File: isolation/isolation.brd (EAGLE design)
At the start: 74.5 x 72.7 mm, 88 parts, among them IC1 XTLV61048DBVR, IC2 SN74HC14PWR, IC3 SN74HCS32BQAR, IC4 SN74HCS08DYYR, IC5 FDN359BN, IC6 FDN359BN, IC7 FDN359BN, IC8 FDN359BN, J1 S4B-PH-K-S(LF)(SN), J2 S4B-PH-K-S(LF)(SN), J3 S2B-PH-K-S(LF)(SN), J4 S2B-PH-K-S(LF)(SN), J5 S2B-PH-K-S(LF)(SN), J6 USB4105-GF-A

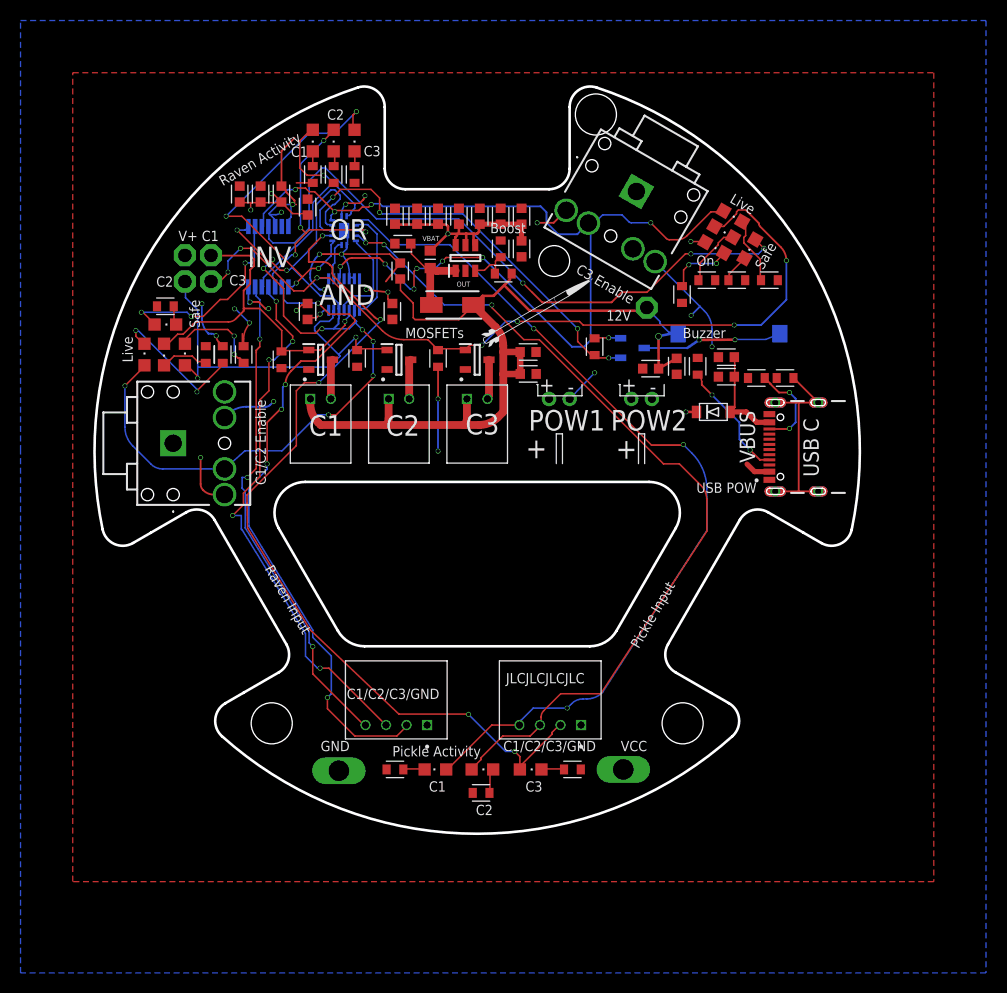
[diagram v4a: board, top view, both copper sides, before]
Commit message: move all components to top
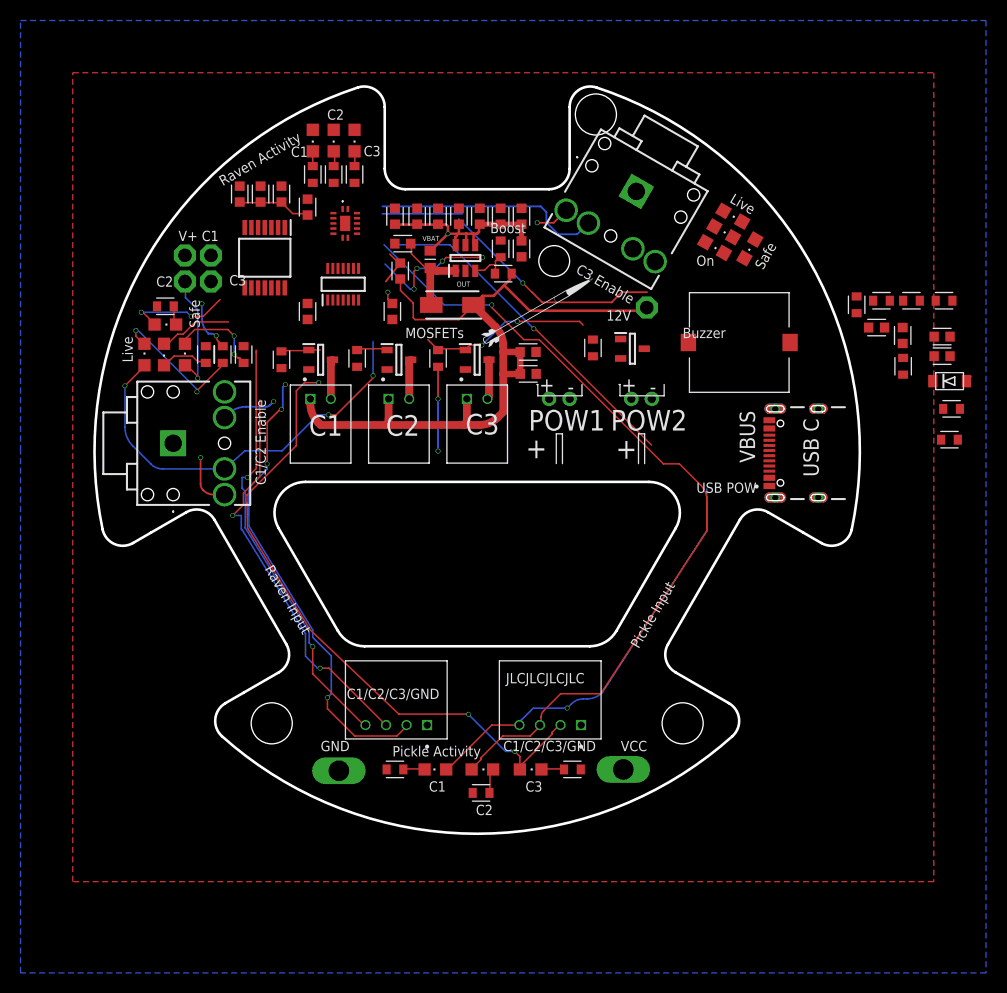
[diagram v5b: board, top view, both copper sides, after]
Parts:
- moved D2 23.2 mm to (46.0, 6.81)
- moved C19 22.4 mm to (38.9, 12.0)
- moved C18 22.2 mm to (41.4, 11.2)
- moved C14 21.1 mm to (45.3, 9.24)
- moved C15 21.1 mm to (45.3, 11.1)
- moved R14 20.0 mm to (41.5, 8.26)
- moved R12 19.2 mm to (46.2, 4.11)
- moved R7 17.1 mm to (42.3, 14.6)
- moved R5 17.1 mm to (45.4, 14.6)
- moved R23 17.1 mm to (39.4, 14.6)
- moved R13 17.1 mm to (46.0, 1.11)
- moved R1 17.0 mm to (36.9, 14.2)
- moved LS1 1.32 mm to (25.5, 10.6), flipped to the top, turned to 90 degrees
- moved IC4 1.00 mm to (-13.0, 16.2), flipped to the top
- moved IC3 0.71 mm to (-12.8, 22.2), flipped to the top
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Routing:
- net EN2: track 99.0 -> 36.0 mm, vias 10 -> 4
- net FIRE3: track 80.7 -> 17.9 mm, vias 7 -> 2
- net GND: track 82.6 -> 22.8 mm, vias 17 -> 5
- net EN1: track 90.7 -> 40.2 mm, vias 10 -> 3
- net SAFE2: track 64.1 -> 22.3 mm, vias 3 -> 1
- net INVR3: track 35.8 -> 0.15 mm, vias 4 -> 0
- net BUZZ: track 41.4 -> 8.10 mm, vias 4 -> 0
- net INVR1: track 26.1 -> 0.52 mm, vias 1 -> 0
- net INVR2: track 25.6 -> 0.18 mm, vias 4 -> 0
- net FIRE2: track 39.7 -> 15.1 mm, vias 2 -> 1
- net FIRE1: track 34.2 -> 11.0 mm, vias 1 -> 0
- net PICKLE3: track 84.5 -> 62.2 mm, vias 5 -> 3
- net SHLD: track 20.4 -> 0.02 mm
- net RAVEN3: track 64.1 -> 45.2 mm, vias 5 -> 4
- net VBAT: track 55.8 -> 40.3 mm, vias 14 -> 4
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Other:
- board text removed: "AND"
- board text removed: "INV"
- board text removed: "OR"

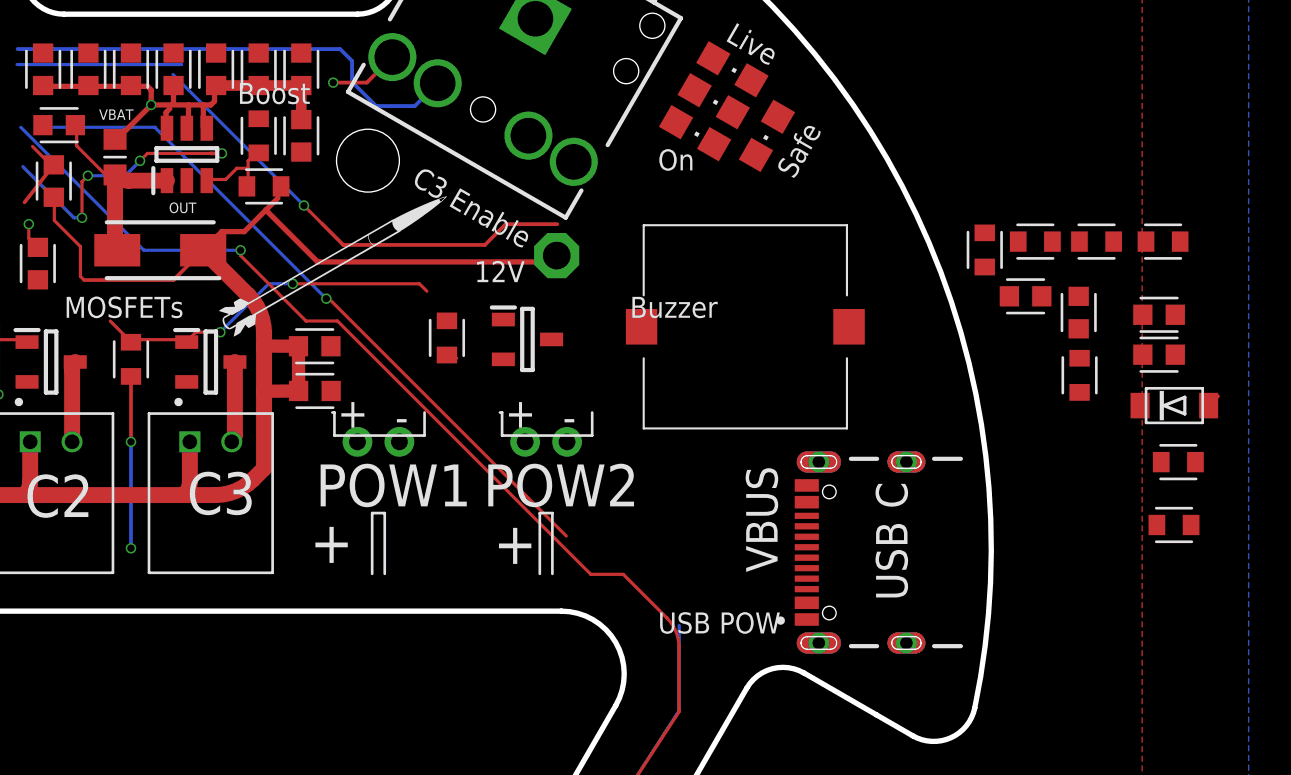
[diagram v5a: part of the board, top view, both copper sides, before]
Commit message: flip all components to top
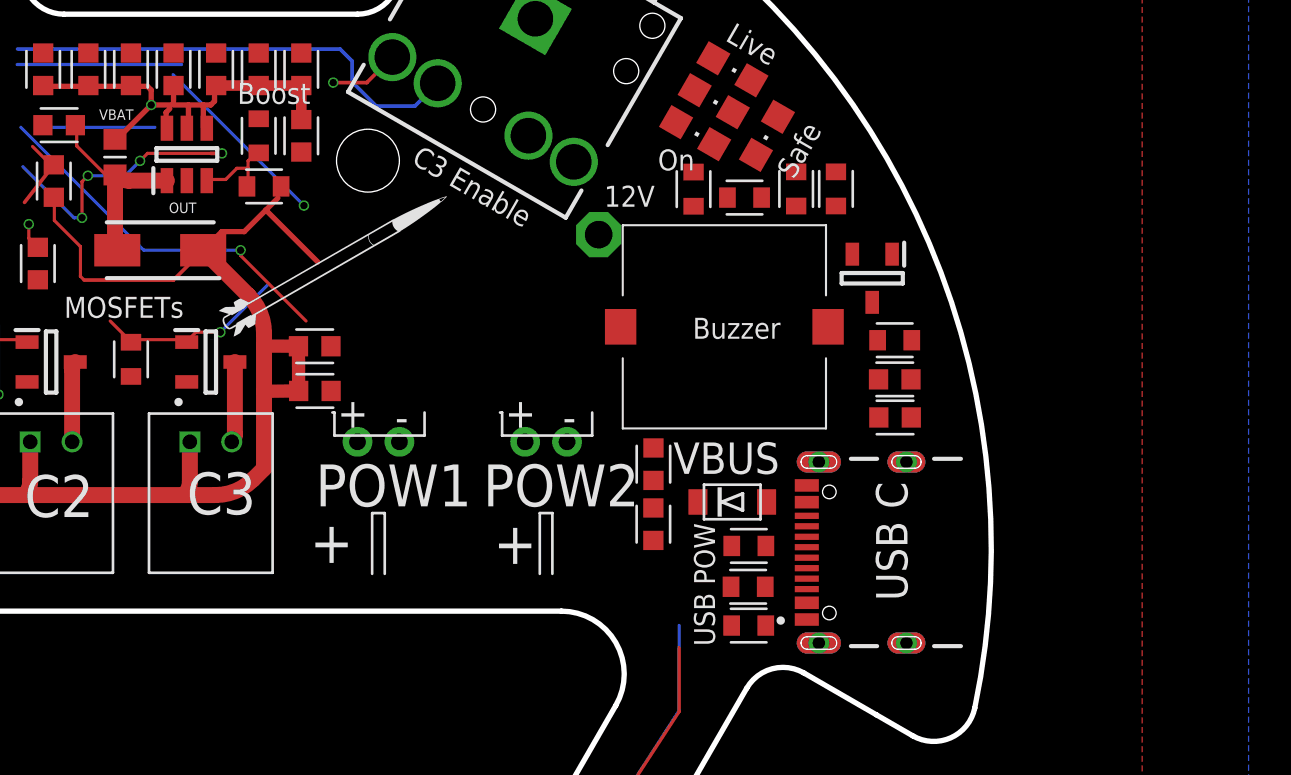
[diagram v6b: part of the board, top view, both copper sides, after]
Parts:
- moved C18 22.7 mm to (21.1, 1.15)
- moved D2 21.6 mm to (24.9, 2.21)
- moved R11 21.4 mm to (32.6, 9.93), turned to 180 degrees
- moved R12 20.9 mm to (25.7, 0.11)
- moved R13 20.9 mm to (25.7, -3.69)
- moved C19 19.5 mm to (21.1, 4.01), turned to 90 degrees
- moved R14 18.8 mm to (25.6, -1.84), turned to 180 degrees
- moved R7 16.9 mm to (25.5, 16.7)
- moved IC8 16.7 mm to (31.6, 12.9), turned to 270 degrees
- moved R5 15.8 mm to (29.8, 17.2), turned to 90 degrees
- moved R1 14.2 mm to (23.0, 17.1)
- moved C15 13.5 mm to (32.7, 6.24), turned to 180 degrees
- moved C14 12.7 mm to (32.6, 8.06), turned to 180 degrees
- moved R23 11.7 mm to (27.9, 17.1), turned to 90 degrees
- moved TP9 2.24 mm to (18.5, 15.0)
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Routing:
- net PICKLE1: track 74.3 -> 46.5 mm, vias 2 -> 1
- net PICKLE2: track 80.6 -> 56.0 mm
- net SAFE2: track 22.3 -> 9.04 mm
- net VDEP: track 73.7 -> 62.6 mm
- net GND: track 22.8 -> 14.5 mm, vias 5 -> 3
- net FIRE3: track 17.9 -> 10.2 mm, vias 2 -> 1
- net VBUS: track 0.91 -> 0.00 mm

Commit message: reset layout
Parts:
- moved C13 3.12 mm to (-9.65, 16.4)
- moved C12 1.27 mm to (-16.5, 12.3), turned to 180 degrees
- moved IC2 1.27 mm to (-20.7, 17.6)
- moved C11 0.36 mm to (-16.3, 24.0)
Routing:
- net VBAT: track 40.3 -> 0.00 mm, vias 4 -> 0
- net EN1: track 40.2 -> 0.00 mm, vias 3 -> 0
- net EN2: track 36.0 -> 0.00 mm, vias 4 -> 0
- net VDEP: track 62.6 -> 39.6 mm
- net PICKLE1: track 46.5 -> 69.0 mm
- net VBUS: track 0.00 -> 16.2 mm
- net SHLD: track 0.00 -> 15.7 mm
- net FIRE2: track 15.1 -> 0.00 mm, vias 1 -> 0
- net GND: track 14.5 -> 0.00 mm, vias 3 -> 0
- net N$5: track 14.1 -> 0.00 mm, vias 2 -> 0
- net PICKLE2: track 56.0 -> 69.1 mm
- net PICKLE3: track 62.2 -> 75.0 mm, vias 3 -> 1
- net FIRE1: track 11.0 -> 0.00 mm
- net SAFE1: track 10.3 -> 0.00 mm, vias 2 -> 0
- net FIRE3: track 10.2 -> 0.00 mm, vias 1 -> 0
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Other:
- outline, holes or cut-outs redrawn

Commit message: reset routing
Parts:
- moved C2 10.2 mm to (2.29, 14.6)
- moved R8 0.13 mm to (-19.1, 9.02)
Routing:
- net VDEP: track 39.6 -> 78.8 mm
- net VBAT: track 0.00 -> 31.1 mm, vias 0 -> 3
- net PICKLE1: track 69.0 -> 79.0 mm
- net N$2: track 0.00 -> 9.71 mm
- net PICKLE2: track 69.1 -> 78.2 mm
- net N$4: track 0.00 -> 7.66 mm
- net PICKLE3: track 75.0 -> 80.9 mm
- net N$13: track 0.00 -> 4.48 mm
- net BUZZ: track 0.00 -> 4.21 mm
- net SHLD: track 15.7 -> 19.9 mm
- net N$3: track 0.00 -> 3.86 mm
- net COM3: track 0.00 -> 3.21 mm
- net FIRE2: track 0.00 -> 2.92 mm
- net FIRE3: track 0.00 -> 2.66 mm
- net FIRE1: track 0.00 -> 2.66 mm
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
